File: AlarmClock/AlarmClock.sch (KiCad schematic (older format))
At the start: 32 parts, among them Q1 2N3904, Q2 2N3904, Q3 2N3904, Q4 2N3904, Q5 2N3904, U1 LM386, U2 LTC-4727JR, U3 LM358

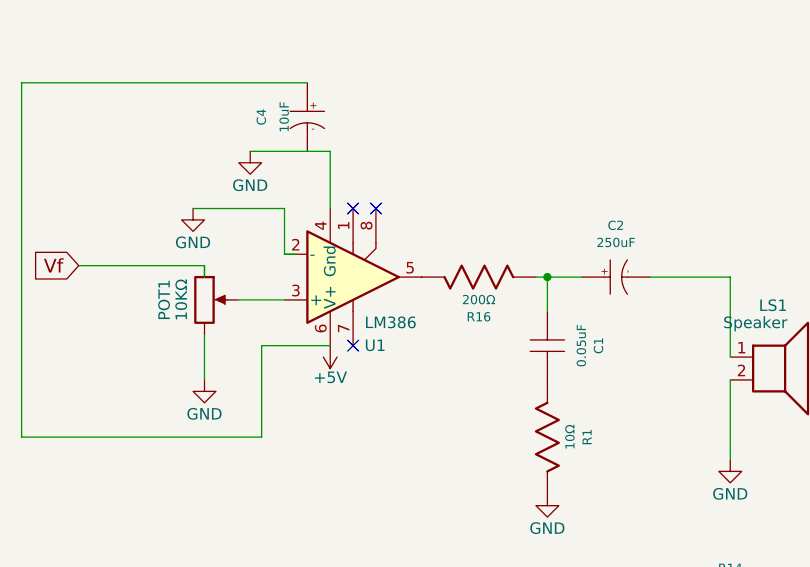
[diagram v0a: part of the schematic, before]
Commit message: Added Footprints
Added footprints to all components except 100kOhm potentiometer, also we need to add push buttons and figure out how they are going to work with the pull up/down resistors in the stm board
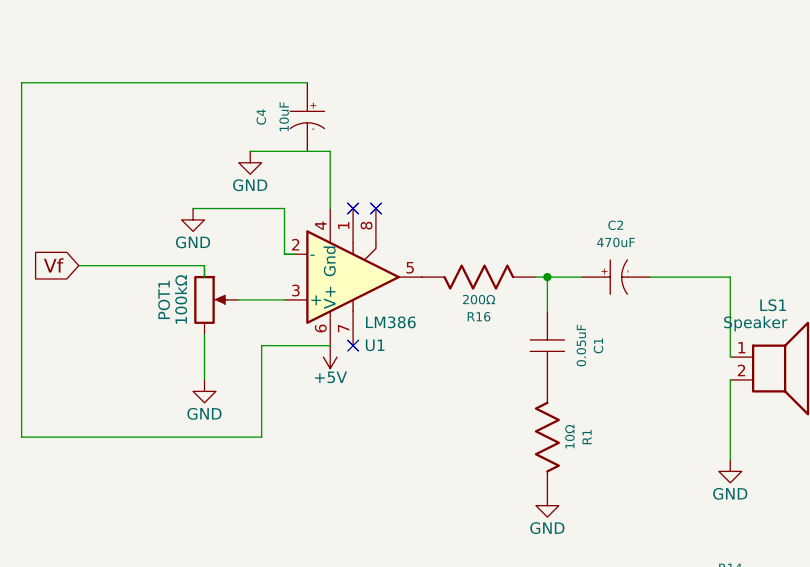
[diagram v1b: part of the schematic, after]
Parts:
- C1, C3, C5: footprint (none) -> ECE:CAP.1
- C2: value 250uF -> 470uF; footprint (none) -> ECE:CAP_Pol_D6.3xH11.5xP2.0mm
- C4: footprint (none) -> ECE:CAP_Pol_D6.3xH11.5xP2.0mm
- LS1: footprint (none) -> Wire_Pads:SolderWirePad_2x_1mmDrill
- POT1: value 10KΩ -> 100kΩ
- Q1, Q2, Q3, Q4, Q5: footprint (none) -> ECE:TO92
- R1, R10, R11, R12, R13, R14, R15, R16, R2, R3, R4, R5, R6, R7, R8, R9: footprint (none) -> ECE:RES.3
- STM1: footprint (none) -> ECE:STM32_F4
- U1, U3: footprint (none) -> ECE:DIP8
- U2: footprint (none) -> ECE:LTC-4727JR

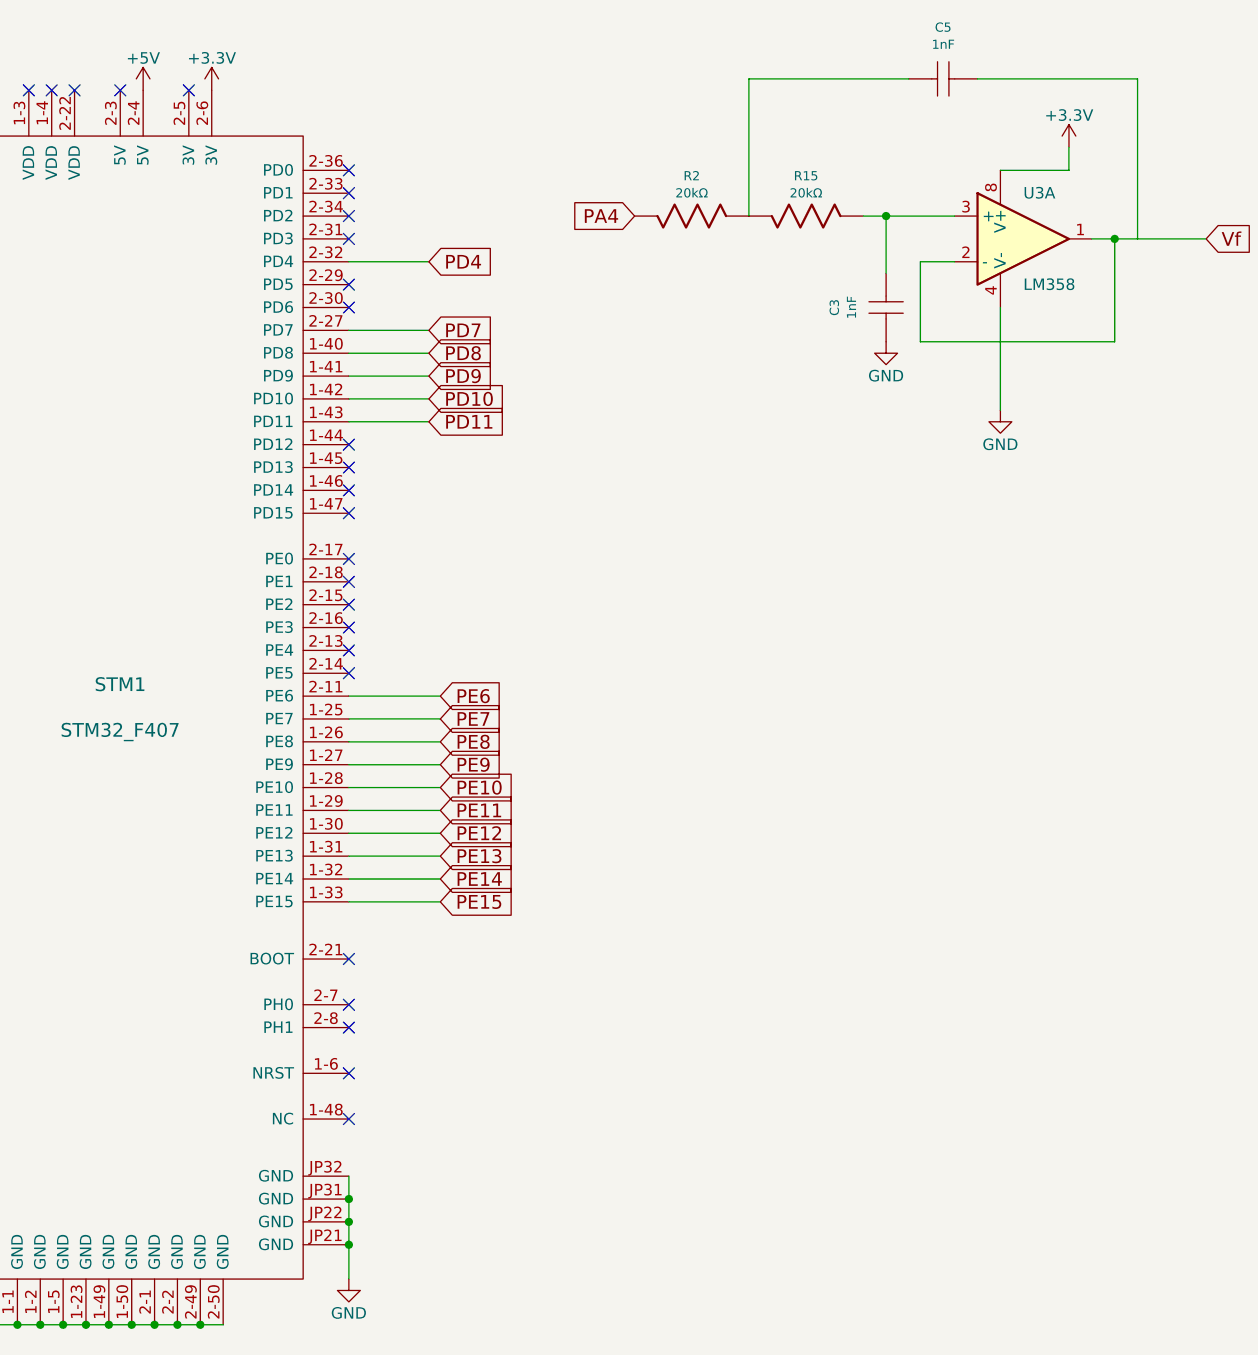
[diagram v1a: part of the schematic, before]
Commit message: added pushbuttons
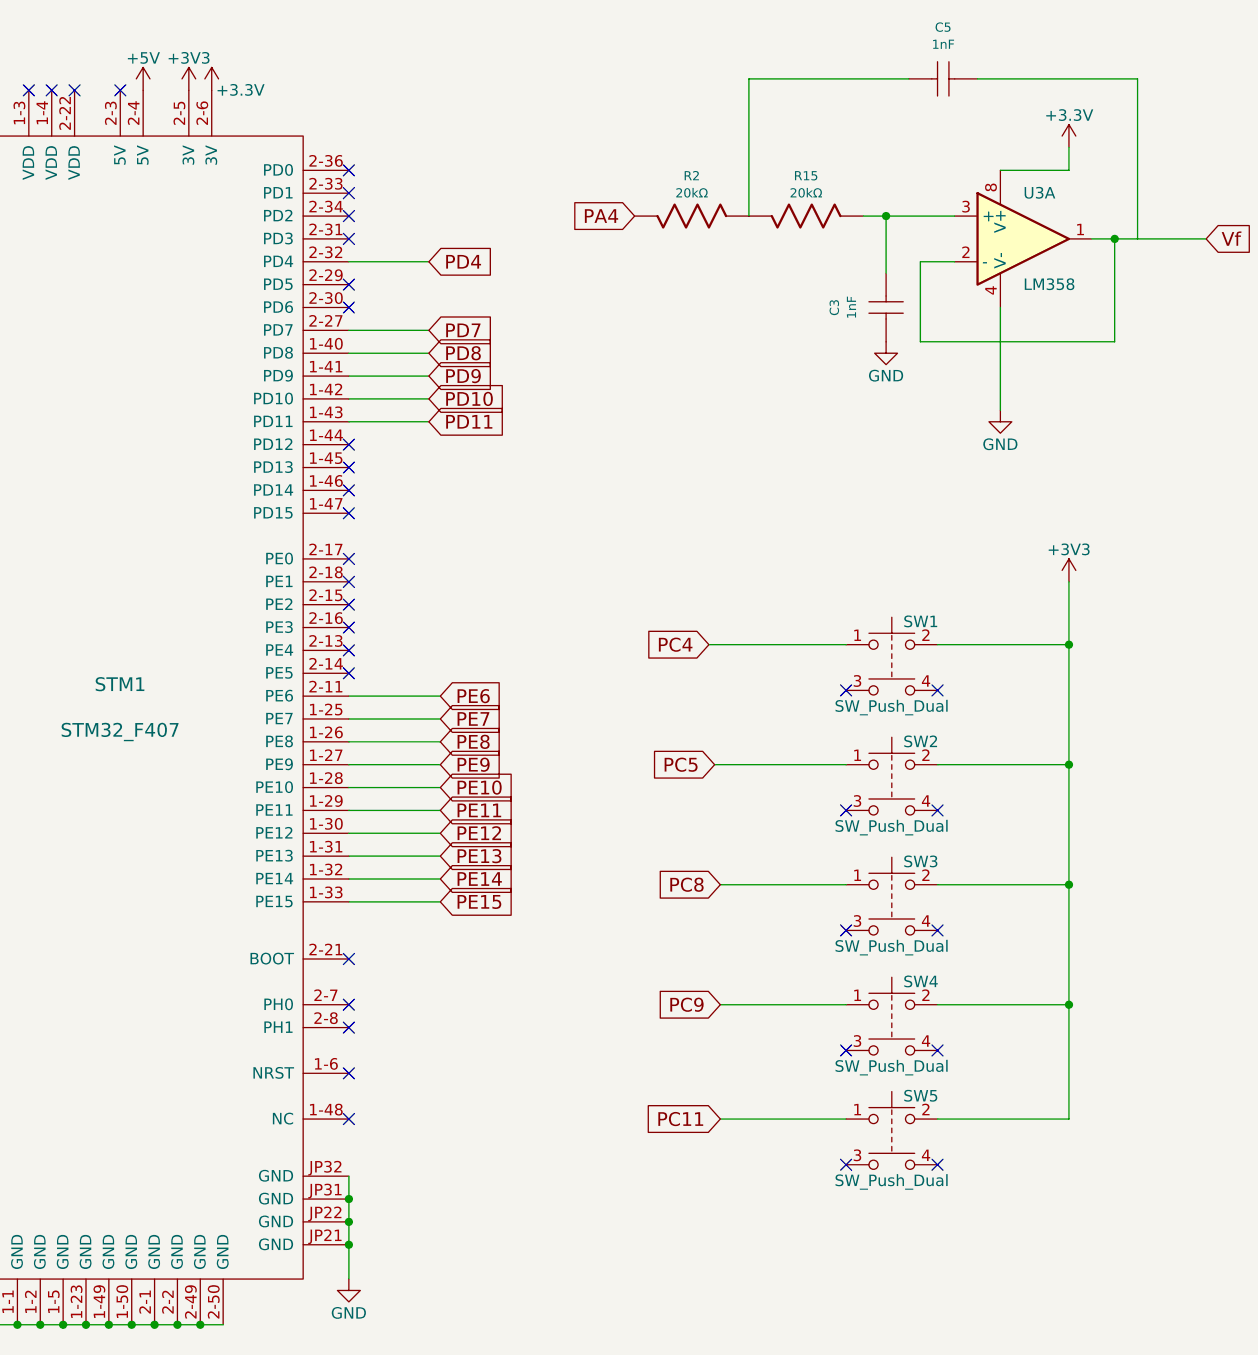
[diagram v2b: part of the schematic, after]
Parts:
- added SW1, SW2, SW3, SW4, SW5: SW_Push_Dual, Buttons_Switches_THT:SW_PUSH_6mm, symbol SW_Push_Dual
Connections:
- net +3V3: now also STM1.2-5 (3V), SW1.2, SW2.2, SW3.2, SW4.2, SW5.2
- net PC11: now also SW5.1
- net PC4: now also SW1.1
- net PC5: now also SW2.1
- net PC8: now also SW3.1
- net PC9: now also SW4.1
- no-connect marks 71 -> 80

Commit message: pcb
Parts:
- added D1, D2: Diode, ECE:DO41, symbol Diode
- POT1: footprint (none) -> Potentiometers:Potentiometer_Alps_RK09K_Horizontal
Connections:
- net +3V3: now also D2.A (Anode); no longer SW1.2, SW2.2, SW3.2, SW4.2, SW5.2
- net GND: now also C4.2 (-)
- net Vf: now also C5.1
- net at C2.2 (-): now also D1.A (Anode); no longer LS1.1
- new net: D1.K (Cathode), LS1.1
- new net: D2.K (Cathode), SW1.2, SW2.2, SW3.2, SW4.2, SW5.2
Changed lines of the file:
@@
 F 0 "POT1" V 1225 2000 50  0000 C CNN
 F 1 "100kΩ" V 1300 2000 50  0000 C CNN
-F 2 "" H 1400 2000 50  0001 C CNN
+F 2 "Potentiometers:Potentiometer_Alps_RK09K_Horizontal" H 1400 2000 50  0001 C CNN
 F 3 "" H 1400 2000 50  0001 C CNN
 	1    1400 2000
@@
 L +3V3 #PWR016
 U 1 1 5B3BFF09
-P 10050 3200
-F 0 "#PWR016" H 10050 3050 50  0001 C CNN
-F 1 "+3V3" H 10050 3340 50  0000 C CNN
-F 2 "" H 10050 3200 50  0001 C CNN
-F 3 "" H 10050 3200 50  0001 C CNN
-	1    10050 3200
+P 10050 3000
+F 0 "#PWR016" H 10050 2850 50  0001 C CNN
+F 1 "+3V3" H 10050 3140 50  0000 C CNN
+F 2 "" H 10050 3000 50  0001 C CNN
+F 3 "" H 10050 3000 50  0001 C CNN
+	1    10050 3000
 	1    0    0    -1
 $EndComp
@@
 	7300 4600 6900 4600
 Wire Wire Line
-	3350 1900 3700 1900
-Wire Wire Line
 	1950 2200 1650 2200
 Wire Wire Line
@@
 	9475 4525 10050 4525
 Connection ~ 10050 4525
-Wire Wire Line
-	10050 3200 10050 5550
 Connection ~ 10050 3475
 Wire Wire Line
@@
 NoConn ~ 9075 5750
 NoConn ~ 9475 5750
+$Comp
+L Diode D1
+U 1 1 5B3C0B12
+P 3500 1900
+F 0 "D1" H 3500 2000 50  0000 C CNN
+F 1 "Diode" H 3500 1800 50  0000 C CNN
+F 2 "ECE:DO41" H 3500 1900 50  0000 C CNN
+F 3 "" H 3500 1900 50  0000 C CNN
+	1    3500 1900
+	-1   0    0    1
+$EndComp
+Wire Wire Line
+	3700 1900 3650 1900
+$Comp
+L Diode D2
+U 1 1 5B3C12E0
+P 10050 3300
+F 0 "D2" H 10050 3400 50  0000 C CNN
+F 1 "Diode" H 10050 3200 50  0000 C CNN
+F 2 "ECE:DO41" H 10050 3300 50  0000 C CNN
+F 3 "" H 10050 3300 50  0000 C CNN
+	1    10050 3300
+	0    -1   -1   0
+$EndComp
+Wire Wire Line
+	10050 3000 10050 3150
+Wire Wire Line
+	10050 3450 10050 5550
+Connection ~ 10350 1700
+Connection ~ 1850 1350
 $EndSCHEMATC

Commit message: geber files and final pcb
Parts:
- removed SW1, SW2, SW3, SW4, SW5: SW_Push_Dual, Buttons_Switches_THT:SW_PUSH_6mm, symbol SW_Push_Dual
- added SW1, SW2, SW3, SW4, SW5: SW_Push, Buttons_Switches_THT:SW_PUSH_6mm, symbol SW_Push
- LS1: footprint Wire_Pads:SolderWirePad_2x_1mmDrill -> Wire_Connections_Bridges:WireConnection_1.00mmDrill
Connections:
- net PC11: now also SW5.1
- net PC4: now also SW1.1
- net PC5: now also SW2.1
- net PC8: now also SW3.1
- net PC9: now also SW4.1
- net at D2.K (Cathode): now also SW1.2, SW2.2, SW3.2, SW4.2, SW5.2
- no-connect marks 80 -> 70
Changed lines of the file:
@@
 F 0 "LS1" H 3950 2475 50  0000 R CNN
 F 1 "Speaker" H 3950 2400 50  0000 R CNN
-F 2 "Wire_Pads:SolderWirePad_2x_1mmDrill" H 3900 2050 50  0001 C CNN
+F 2 "Wire_Connections_Bridges:WireConnection_1.00mmDrill" H 3900 2050 50  0001 C CNN
 F 3 "" H 3890 2200 50  0001 C CNN
 	1    3900 2250
@@
 $EndComp
 $Comp
-L SW_Push_Dual SW1
-U 1 1 5B3BDA0C
-P 9275 3475
-F 0 "SW1" H 9325 3575 50  0000 L CNN
-F 1 "SW_Push_Dual" H 9275 3205 50  0000 C CNN
-F 2 "Buttons_Switches_THT:SW_PUSH_6mm" H 9275 3675 50  0001 C CNN
-F 3 "" H 9275 3675 50  0001 C CNN
-	1    9275 3475
-	1    0    0    -1
-$EndComp
-$Comp
-L SW_Push_Dual SW2
-U 1 1 5B3BDD20
-P 9275 4000
-F 0 "SW2" H 9325 4100 50  0000 L CNN
-F 1 "SW_Push_Dual" H 9275 3730 50  0000 C CNN
-F 2 "Buttons_Switches_THT:SW_PUSH_6mm" H 9275 4200 50  0001 C CNN
-F 3 "" H 9275 4200 50  0001 C CNN
-	1    9275 4000
-	1    0    0    -1
-$EndComp
-$Comp
-L SW_Push_Dual SW3
-U 1 1 5B3BDD87
-P 9275 4525
-F 0 "SW3" H 9325 4625 50  0000 L CNN
-F 1 "SW_Push_Dual" H 9275 4255 50  0000 C CNN
-F 2 "Buttons_Switches_THT:SW_PUSH_6mm" H 9275 4725 50  0001 C CNN
-F 3 "" H 9275 4725 50  0001 C CNN
-	1    9275 4525
-	1    0    0    -1
-$EndComp
-$Comp
-L SW_Push_Dual SW4
-U 1 1 5B3BDEC7
-P 9275 5050
-F 0 "SW4" H 9325 5150 50  0000 L CNN
-F 1 "SW_Push_Dual" H 9275 4780 50  0000 C CNN
-F 2 "Buttons_Switches_THT:SW_PUSH_6mm" H 9275 5250 50  0001 C CNN
-F 3 "" H 9275 5250 50  0001 C CNN
-	1    9275 5050
-	1    0    0    -1
-$EndComp
-$Comp
-L SW_Push_Dual SW5
-U 1 1 5B3BE993
-P 9275 5550
-F 0 "SW5" H 9325 5650 50  0000 L CNN
-F 1 "SW_Push_Dual" H 9275 5280 50  0000 C CNN
-F 2 "Buttons_Switches_THT:SW_PUSH_6mm" H 9275 5750 50  0001 C CNN
-F 3 "" H 9275 5750 50  0001 C CNN
-	1    9275 5550
-	1    0    0    -1
-$EndComp
-$Comp
 L +3V3 #PWR015
 U 1 1 5B3BF19D
@@
 Wire Wire Line
 	9075 3475 8475 3475
-NoConn ~ 9075 3675
-NoConn ~ 9475 3675
-NoConn ~ 9075 4200
-NoConn ~ 9475 4200
-NoConn ~ 9075 4725
-NoConn ~ 9475 4725
-NoConn ~ 9075 5250
-NoConn ~ 9475 5250
-NoConn ~ 9075 5750
-NoConn ~ 9475 5750
 $Comp
 L Diode D1
@@
 Connection ~ 10350 1700
 Connection ~ 1850 1350
+$Comp
+L SW_Push SW1
+U 1 1 5B3C2F2D
+P 9275 3475
+F 0 "SW1" H 9325 3575 50  0000 L CNN
+F 1 "SW_Push" H 9275 3415 50  0000 C CNN
+F 2 "Buttons_Switches_THT:SW_PUSH_6mm" H 9275 3675 50  0001 C CNN
+F 3 "" H 9275 3675 50  0001 C CNN
+	1    9275 3475
+	1    0    0    -1
+$EndComp
+$Comp
+L SW_Push SW2
+U 1 1 5B3C2FB8
+P 9275 4000
+F 0 "SW2" H 9325 4100 50  0000 L CNN
+F 1 "SW_Push" H 9275 3940 50  0000 C CNN
+F 2 "Buttons_Switches_THT:SW_PUSH_6mm" H 9275 4200 50  0001 C CNN
+F 3 "" H 9275 4200 50  0001 C CNN
+	1    9275 4000
+	1    0    0    -1
+$EndComp
+$Comp
+L SW_Push SW3
+U 1 1 5B3C301B
+P 9275 4525
+F 0 "SW3" H 9325 4625 50  0000 L CNN
+F 1 "SW_Push" H 9275 4465 50  0000 C CNN
+F 2 "Buttons_Switches_THT:SW_PUSH_6mm" H 9275 4725 50  0001 C CNN
+F 3 "" H 9275 4725 50  0001 C CNN
+	1    9275 4525
+	1    0    0    -1
+$EndComp
+$Comp
+L SW_Push SW4
+U 1 1 5B3C30A4
+P 9275 5050
+F 0 "SW4" H 9325 5150 50  0000 L CNN
+F 1 "SW_Push" H 9275 4990 50  0000 C CNN
+F 2 "Buttons_Switches_THT:SW_PUSH_6mm" H 9275 5250 50  0001 C CNN
+F 3 "" H 9275 5250 50  0001 C CNN
+	1    9275 5050
+	1    0    0    -1
+$EndComp
+$Comp
+L SW_Push SW5
+U 1 1 5B3C3113
+P 9275 5550
+F 0 "SW5" H 9325 5650 50  0000 L CNN
+F 1 "SW_Push" H 9275 5490 50  0000 C CNN
+F 2 "Buttons_Switches_THT:SW_PUSH_6mm" H 9275 5750 50  0001 C CNN
+F 3 "" H 9275 5750 50  0001 C CNN
+	1    9275 5550
+	1    0    0    -1
+$EndComp
 $EndSCHEMATC
